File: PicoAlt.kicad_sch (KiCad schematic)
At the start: 40 parts, among them J2 USB_B, J3 Conn_01x04, J4 Conn_01x20, J5 Conn_01x20, SW1 SW_Push, SW2 SW_Push, U1 AMS1117-3.3, U2 W25Q128JVSIQ, U3 RP2350, Y1 12 MHz

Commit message: rearranged layout
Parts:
- added C6: 4.7 uF, Capacitor_SMD:C_0603_1608Metric, symbol Device:C_Small
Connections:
- net +1V1: now also C6.1
- net GND: now also C6.2
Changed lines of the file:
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@@
   (junction (at 26.67 158.115) (diameter 0) (color 0 0 0 0)
   )
+  (junction (at 50.8 158.115) (diameter 0) (color 0 0 0 0)
+  )
   (junction (at 241.3 85.725) (diameter 0) (color 0 0 0 0)
   )
@@
   (junction (at 118.11 50.8) (diameter 0) (color 0 0 0 0)
   )
+  (junction (at 50.8 163.83) (diameter 0) (color 0 0 0 0)
+  )
   (junction (at 149.86 48.26) (diameter 0) (color 0 0 0 0)
   )
@@
     (stroke (width 0) (type default) (color 0 0 0 0))
   )
-  (wire (pts (xy 40.005 163.83) (xy 64.77 163.83))
+  (wire (pts (xy 40.005 163.83) (xy 50.8 163.83))
     (stroke (width 0) (type default) (color 0 0 0 0))
   )
@@
     (stroke (width 0) (type default) (color 0 0 0 0))
   )
-  (wire (pts (xy 40.005 158.115) (xy 64.77 158.115))
+  (wire (pts (xy 40.005 158.115) (xy 50.8 158.115))
     (stroke (width 0) (type default) (color 0 0 0 0))
   )
@@
     (stroke (width 0) (type default) (color 0 0 0 0))
   )
+  (wire (pts (xy 50.8 163.83) (xy 64.77 163.83))
+    (stroke (width 0) (type default) (color 0 0 0 0))
+  )
   (wire (pts (xy 144.78 48.26) (xy 144.78 50.8))
     (stroke (width 0) (type default) (color 0 0 0 0))
@@
   )
   (wire (pts (xy 34.29 125.73) (xy 45.085 125.73))
+    (stroke (width 0) (type default) (color 0 0 0 0))
+  )
+  (wire (pts (xy 50.8 163.195) (xy 50.8 163.83))
+    (stroke (width 0) (type default) (color 0 0 0 0))
+  )
+  (wire (pts (xy 50.8 158.115) (xy 64.77 158.115))
     (stroke (width 0) (type default) (color 0 0 0 0))
   )
@@
     (pin "4")
   )
+  (symbol (lib_id "Device:C_Small") (at 50.8 160.655 0) (unit 1)
+    (in_bom yes) (on_board yes)
+    (property "Reference" "C6" (id 0) (at 45.72 160.02 0)
+      (effects (font (size 1.27 1.27)) (justify left))
+    )
+    (property "Value" "4.7 uF" (id 1) (at 53.467 160.528 0)
+      (effects (font (size 1.27 1.27)) (justify left))
+    )
+    (property "Footprint" "Capacitor_SMD:C_0603_1608Metric" (id 2) (at 50.8 160.655 0)
+      (effects (font (size 1.27 1.27)) hide)
+    )
+    (property "Datasheet" "~" (id 3) (at 50.8 160.655 0)
+      (effects (font (size 1.27 1.27)) hide)
+    )
+    (property "LCSC" "C19666" (id 4) (at 50.8 160.655 0)
+      (effects (font (size 1.27 1.27)) hide)
+    )
+    (pin "1")
+    (pin "2")
+  )
   (symbol (lib_id "power:GND") (at 91.186 159.893 0) (unit 1)
     (in_bom yes) (on_board yes) (fields_autoplaced)
@@
       (reference "C5") (unit 1) (value "4.7 uF") (footprint "Capacitor_SMD:C_0603_1608Metric")
     )
+    (path "/9095260a-5072-4f3a-97b4-75eabbc6e60d"
+      (reference "C6") (unit 1) (value "4.7 uF") (footprint "Capacitor_SMD:C_0603_1608Metric")
+    )
     (path "/72753b90-9b55-41e3-a30d-e6e3f40a6a1c"

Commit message: Small modifications of placement
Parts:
- L1: LCSC C98331 -> C162585
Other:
- note added: "NOTE TO SELF: INDUCTOR C2049407 ASMPM-0806-3R3M-T WHEN AVAILABLE"
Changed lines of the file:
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@@
+    (effects (font (size 1.27 1.27)) (justify left bottom))
+  )
+  (text "NOTE TO SELF: INDUCTOR\nC2049407 ASMPM-0806-3R3M-T \nWHEN AVAILABLE"
+    (at 97.155 21.59 0)
     (effects (font (size 1.27 1.27)) (justify left bottom))
   )
@@
       (effects (font (size 1.27 1.27)) hide)
     )
-    (property "LCSC" "C98331" (id 4) (at 129.54 36.83 0)
-      (effects (font (size 1.27 1.27)) hide)
-    )
+    (property "LCSC" "C162585" (id 4) (at 129.54 36.83 0)
+      (effects (font (size 1.27 1.27)) hide)
+    )

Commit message: regulator work
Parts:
- added C20: 4.7 uF, Capacitor_SMD:C_0603_1608Metric, symbol Device:C_Small
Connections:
- net +3.3V: now also C20.1
- net GND: now also C20.2
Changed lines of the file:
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@@
   (junction (at 241.3 85.725) (diameter 0) (color 0 0 0 0)
   )
+  (junction (at 26.035 125.73) (diameter 0) (color 0 0 0 0)
+  )
   (junction (at 109.22 121.92) (diameter 0) (color 0 0 0 0)
   )
@@
   (junction (at 93.98 110.49) (diameter 0) (color 0 0 0 0)
   )
+  (junction (at 26.035 118.11) (diameter 0) (color 0 0 0 0)
+  )
   (junction (at 158.75 36.83) (diameter 0) (color 0 0 0 0)
   )
@@
     (stroke (width 0) (type default) (color 0 0 0 0))
   )
+  (wire (pts (xy 26.035 118.11) (xy 26.035 120.65))
+    (stroke (width 0) (type default) (color 0 0 0 0))
+  )
   (wire (pts (xy 129.54 43.18) (xy 129.54 50.8))
     (stroke (width 0) (type default) (color 0 0 0 0))
@@
     (stroke (width 0) (type default) (color 0 0 0 0))
   )
+  (wire (pts (xy 26.035 125.73) (xy 34.29 125.73))
+    (stroke (width 0) (type default) (color 0 0 0 0))
+  )
   (wire (pts (xy 138.43 45.085) (xy 138.43 48.26))
     (stroke (width 0) (type default) (color 0 0 0 0))
@@
     (stroke (width 0) (type default) (color 0 0 0 0))
   )
-  (wire (pts (xy 14.605 118.11) (xy 34.29 118.11))
+  (wire (pts (xy 14.605 118.11) (xy 26.035 118.11))
     (stroke (width 0) (type default) (color 0 0 0 0))
   )
@@
     (stroke (width 0) (type default) (color 0 0 0 0))
   )
+  (wire (pts (xy 26.035 118.11) (xy 34.29 118.11))
+    (stroke (width 0) (type default) (color 0 0 0 0))
+  )
   (wire (pts (xy 254 65.405) (xy 238.76 65.405))
     (stroke (width 0) (type default) (color 0 0 0 0))
@@
     (stroke (width 0) (type default) (color 0 0 0 0))
   )
-  (wire (pts (xy 14.605 125.73) (xy 34.29 125.73))
+  (wire (pts (xy 14.605 125.73) (xy 26.035 125.73))
     (stroke (width 0) (type default) (color 0 0 0 0))
   )
@@
     (pin "9")
   )
+  (symbol (lib_id "Device:C_Small") (at 26.035 123.19 0) (unit 1)
+    (in_bom yes) (on_board yes)
+    (property "Reference" "C20" (id 0) (at 20.955 122.555 0)
+      (effects (font (size 1.27 1.27)) (justify left))
+    )
+    (property "Value" "4.7 uF" (id 1) (at 28.702 123.063 0)
+      (effects (font (size 1.27 1.27)) (justify left))
+    )
+    (property "Footprint" "Capacitor_SMD:C_0603_1608Metric" (id 2) (at 26.035 123.19 0)
+      (effects (font (size 1.27 1.27)) hide)
+    )
+    (property "Datasheet" "~" (id 3) (at 26.035 123.19 0)
+      (effects (font (size 1.27 1.27)) hide)
+    )
+    (property "LCSC" "C19666" (id 4) (at 26.035 123.19 0)
+      (effects (font (size 1.27 1.27)) hide)
+    )
+    (pin "1")
+    (pin "2")
+  )
   (symbol (lib_id "Device:Crystal_GND24_Small") (at 96.52 106.68 270) (unit 1)
     (in_bom yes) (on_board yes)
@@
       (reference "C19") (unit 1) (value "100 nF") (footprint "Capacitor_SMD:C_0402_1005Metric")
     )
+    (path "/8c1346e0-8e88-41ce-a921-357867244807"
+      (reference "C20") (unit 1) (value "4.7 uF") (footprint "Capacitor_SMD:C_0603_1608Metric")
+    )
     (path "/39dd035f-0f97-493f-924b-700658a8bbb3"

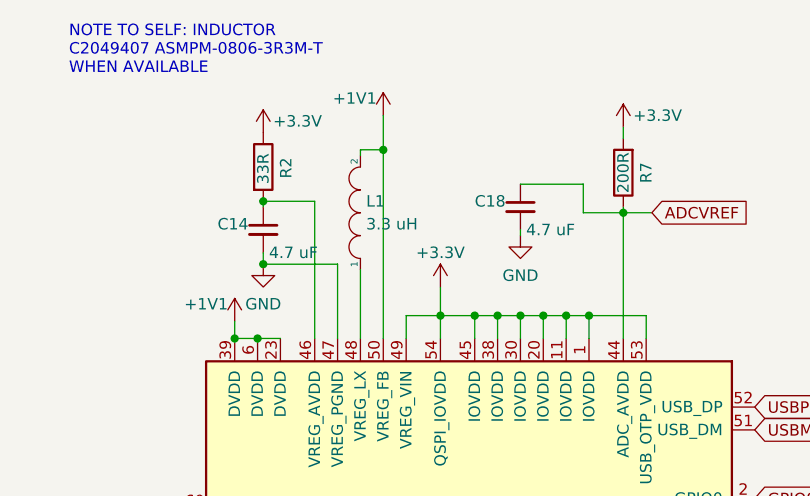
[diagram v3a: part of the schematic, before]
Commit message: Changed inductor
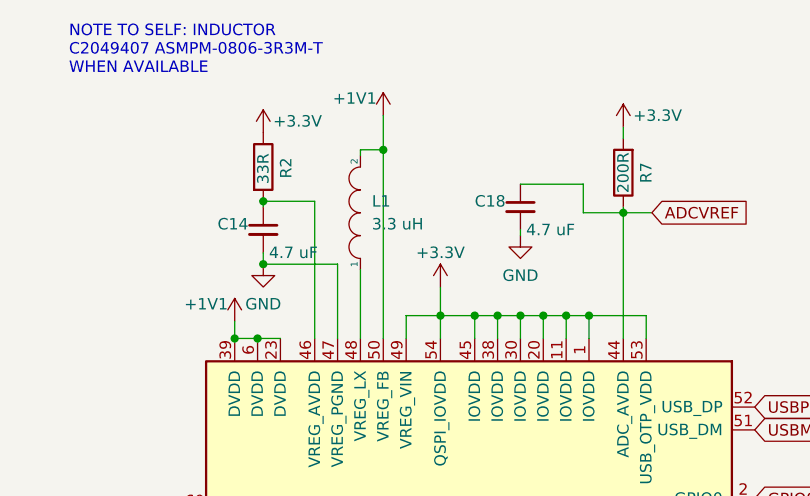
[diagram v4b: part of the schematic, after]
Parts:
- L1: footprint Inductor_SMD:L_0805_2012Metric -> PicoAlt:Inductor_SMD_3x3mm; LCSC C162585 -> C411371
- U2: LCSC (none) -> C97521
- U3: LCSC (none) -> C9900136558
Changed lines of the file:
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@@
+      (effects (font (size 1.27 1.27)) hide)
+    )
+    (property "LCSC" "C97521" (id 4) (at 92.456 179.578 0)
       (effects (font (size 1.27 1.27)) hide)
     )
@@
     )
     (property "Datasheet" "" (id 3) (at 122.555 101.6 0)
+      (effects (font (size 1.27 1.27)) hide)
+    )
+    (property "LCSC" "C9900136558" (id 4) (at 141.605 101.6 0)
       (effects (font (size 1.27 1.27)) hide)
     )
@@
   (symbol (lib_id "pspice:INDUCTOR") (at 129.54 36.83 90) (unit 1)
     (in_bom yes) (on_board yes) (fields_autoplaced)
-    (property "Reference" "L1" (id 0) (at 130.175 35.5599 90)
+    (property "Reference" "L1" (id 0) (at 130.81 35.5599 90)
       (effects (font (size 1.27 1.27)) (justify right))
     )
-    (property "Value" "3.3 uH" (id 1) (at 130.175 38.0999 90)
+    (property "Value" "3.3 uH" (id 1) (at 130.81 38.0999 90)
       (effects (font (size 1.27 1.27)) (justify right))
     )
-    (property "Footprint" "Inductor_SMD:L_0805_2012Metric" (id 2) (at 129.54 36.83 0)
+    (property "Footprint" "PicoAlt:Inductor_SMD_3x3mm" (id 2) (at 129.54 36.83 0)
       (effects (font (size 1.27 1.27)) hide)
     )
@@
       (effects (font (size 1.27 1.27)) hide)
     )
-    (property "LCSC" "C162585" (id 4) (at 129.54 36.83 0)
+    (property "LCSC" "C411371" (id 4) (at 129.54 36.83 0)
       (effects (font (size 1.27 1.27)) hide)
     )
@@
     )
     (path "/a75f3906-0fde-4354-bee0-7f25562cbd72"
-      (reference "L1") (unit 1) (value "3.3 uH") (footprint "Inductor_SMD:L_0805_2012Metric")
+      (reference "L1") (unit 1) (value "3.3 uH") (footprint "PicoAlt:Inductor_SMD_3x3mm")
     )
     (path "/91360d2d-cc65-4a74-a608-518ef882cb51"

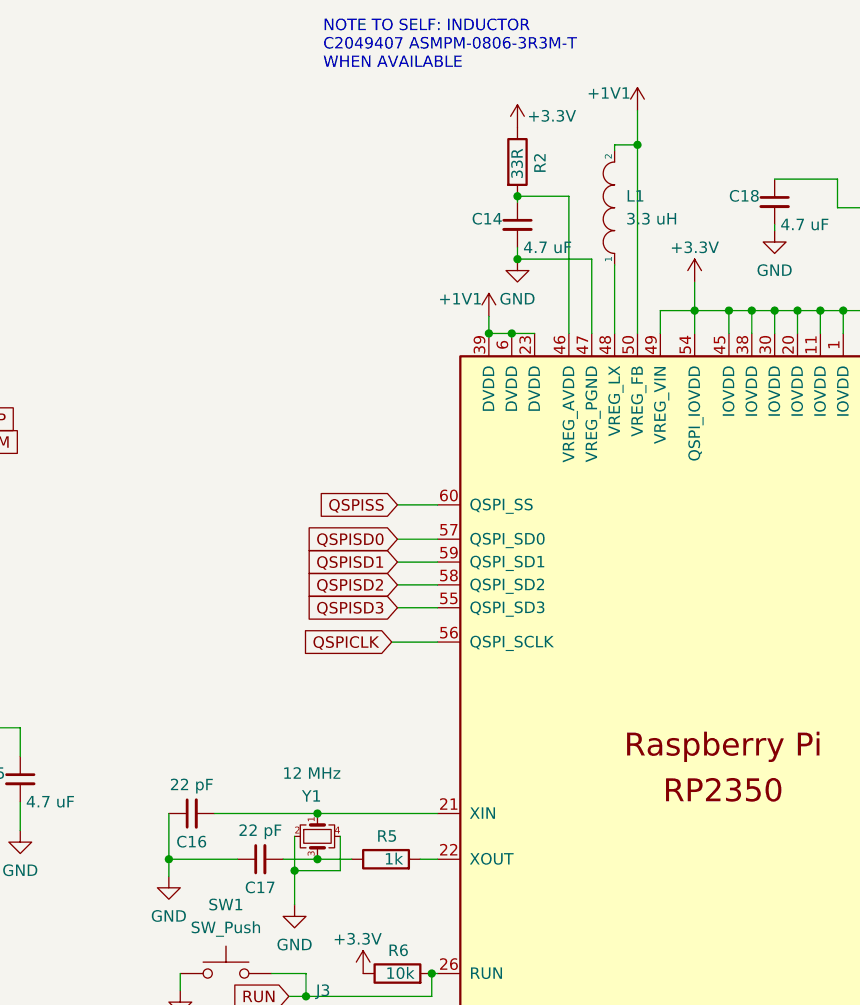
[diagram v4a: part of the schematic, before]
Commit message: Modified for Abracon inductor and oscillator, sent to JLCPCB
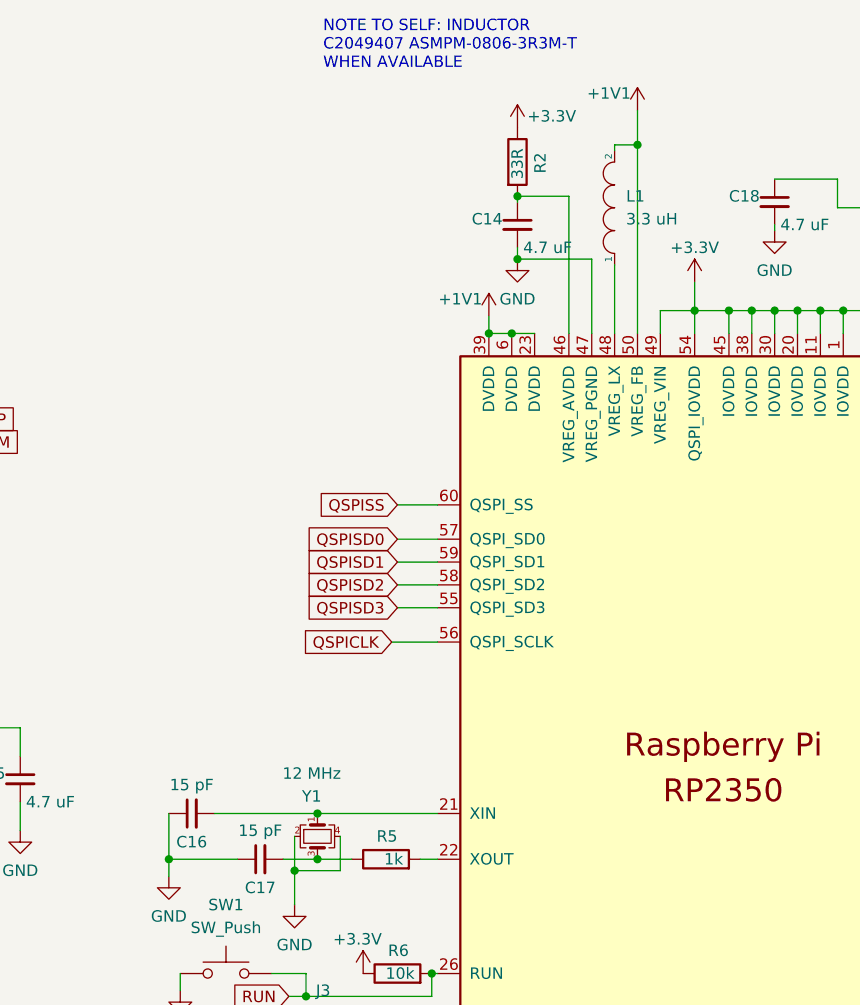
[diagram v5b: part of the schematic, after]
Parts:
- C16, C17: value 22 pF -> 15 pF; LCSC C1555 -> C1548
- L1: footprint PicoAlt:Inductor_SMD_3x3mm -> PicoAlt:Abracon_Pico_inductor; LCSC C411371 -> C42411119
- U3: LCSC C9900136558 -> C42411118
- Y1: LCSC C9002 -> C20625731
